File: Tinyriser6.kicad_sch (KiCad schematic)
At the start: 25 parts, among them J1 Bus_M.2_Socket_M, J2 Bus_PCI_Express_x16, J3 Conn_02x04_Odd_Even, M1 Fan_4pin

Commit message: started breaking out all the weird pins
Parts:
- removed TP1: GPU_PWR_EN, TestPoint:TestPoint_Pad_D1.0mm, symbol Connector:TestPoint
- removed TP2: GPU_MACO_EN, TestPoint:TestPoint_Pad_D1.0mm, symbol Connector:TestPoint
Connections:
- net PCIe_CPU_REFCLK1-: now reaches J4.A1 (PCIe_CPU_REFCLK1-)
- net PCIe_CPU_REFCLK5+: now reaches J4.A17 (PCIe_CPU_REFCLK5+)
- net PCIe_CPU_REFCLK5-: now reaches J4.A18 (PCIe_CPU_REFCLK5-)
- net GPU_PWR_EN: now reaches J4.A19 (GPU_PWR_EN)
- net PCIe_CPU_REFCLK1+: now reaches J4.A2 (PCIe_CPU_REFCLK1+)
- net GPU_MACO_EN: now reaches J4.A20 (GPU_MACO_EN)
- net AZ_SDOUT_R: now reaches J4.A21 (AZ_SDOUT_R(ME_DISABLE))
- net ESPI_ALERT0#_BMC: now reaches J4.A22 (ESPI_ALERT0#_BMC@)
- net ESPI_ALERT1#: now reaches J4.A23 (ESPI_ALERT1#@)
- net SIO_SML1ALERT#: now reaches J4.A24 (SIO_SML1ALERT#)
- net ESPI_IO1_BMC: now reaches J4.A25 (ESPI_IO1_BMC@)
- net ESPI_RESET#_BMC: now reaches J4.A26 (ESPI_RESET#_BMC@)
- net ME_RECOVERY_BMC: now reaches J4.A27 (ME_RECOVERY_BMC)
- net SMLINK1_DATA: now reaches J4.A28 (SMLINK1_DATA)
- net SMLINK1_CLK: now reaches J4.A29 (SMLINK1_CLK)
- net PCH_SYSPOWEROK: now reaches J4.A3 (PCH_SYSPOWEROK)
- net PCIE_X8_X4_PRSNT#: now reaches J4.A30 (PCIE_X8_X4_PRSNT#)
- net ESPI_IO0_BMC: now reaches J4.A31 (ESPI_IO0_BMC@)
- net ESPI_CLK_BMC: now reaches J4.A32 (ESPI_CLK_BMC@)
- net BMC_DETECT#: now reaches J4.A4 (BMC_DETECT#(CLKREQ1,5,11,CFG6)@)
- net ESPI_CS1#_BMC: now reaches J4.B1 (@ESPI_CS1#_BMC)
- net ESPI_CS0#_BMC: now reaches J4.B2 (@ESPI_CS0#_BMC)
- net PCIe_CPU_REFCLK11-: now reaches J4.B23 (PCIe_CPU_REFCLK11-)
- net PCIe_CPU_REFCLK11+: now reaches J4.B24 (PCIe_CPU_REFCLK11+)
- net PWRBTN#: now reaches J4.B25 (PWRBTN#)
- net USB_D-: now reaches J4.B26 (USB_D-)
- net USB_D+: now reaches J4.B27 (USB_D+)
- net FP_RST#: now reaches J4.B28 (FP_RST#)
- net +5V: now reaches J4.B3 (+5V_S5)
- net +5V: now also J4.B4 (+5V_S5), J4.B5 (+5V_S5)
- net RSMRST_SIO#: now reaches J4.B6 (RSMRST_SIO#)

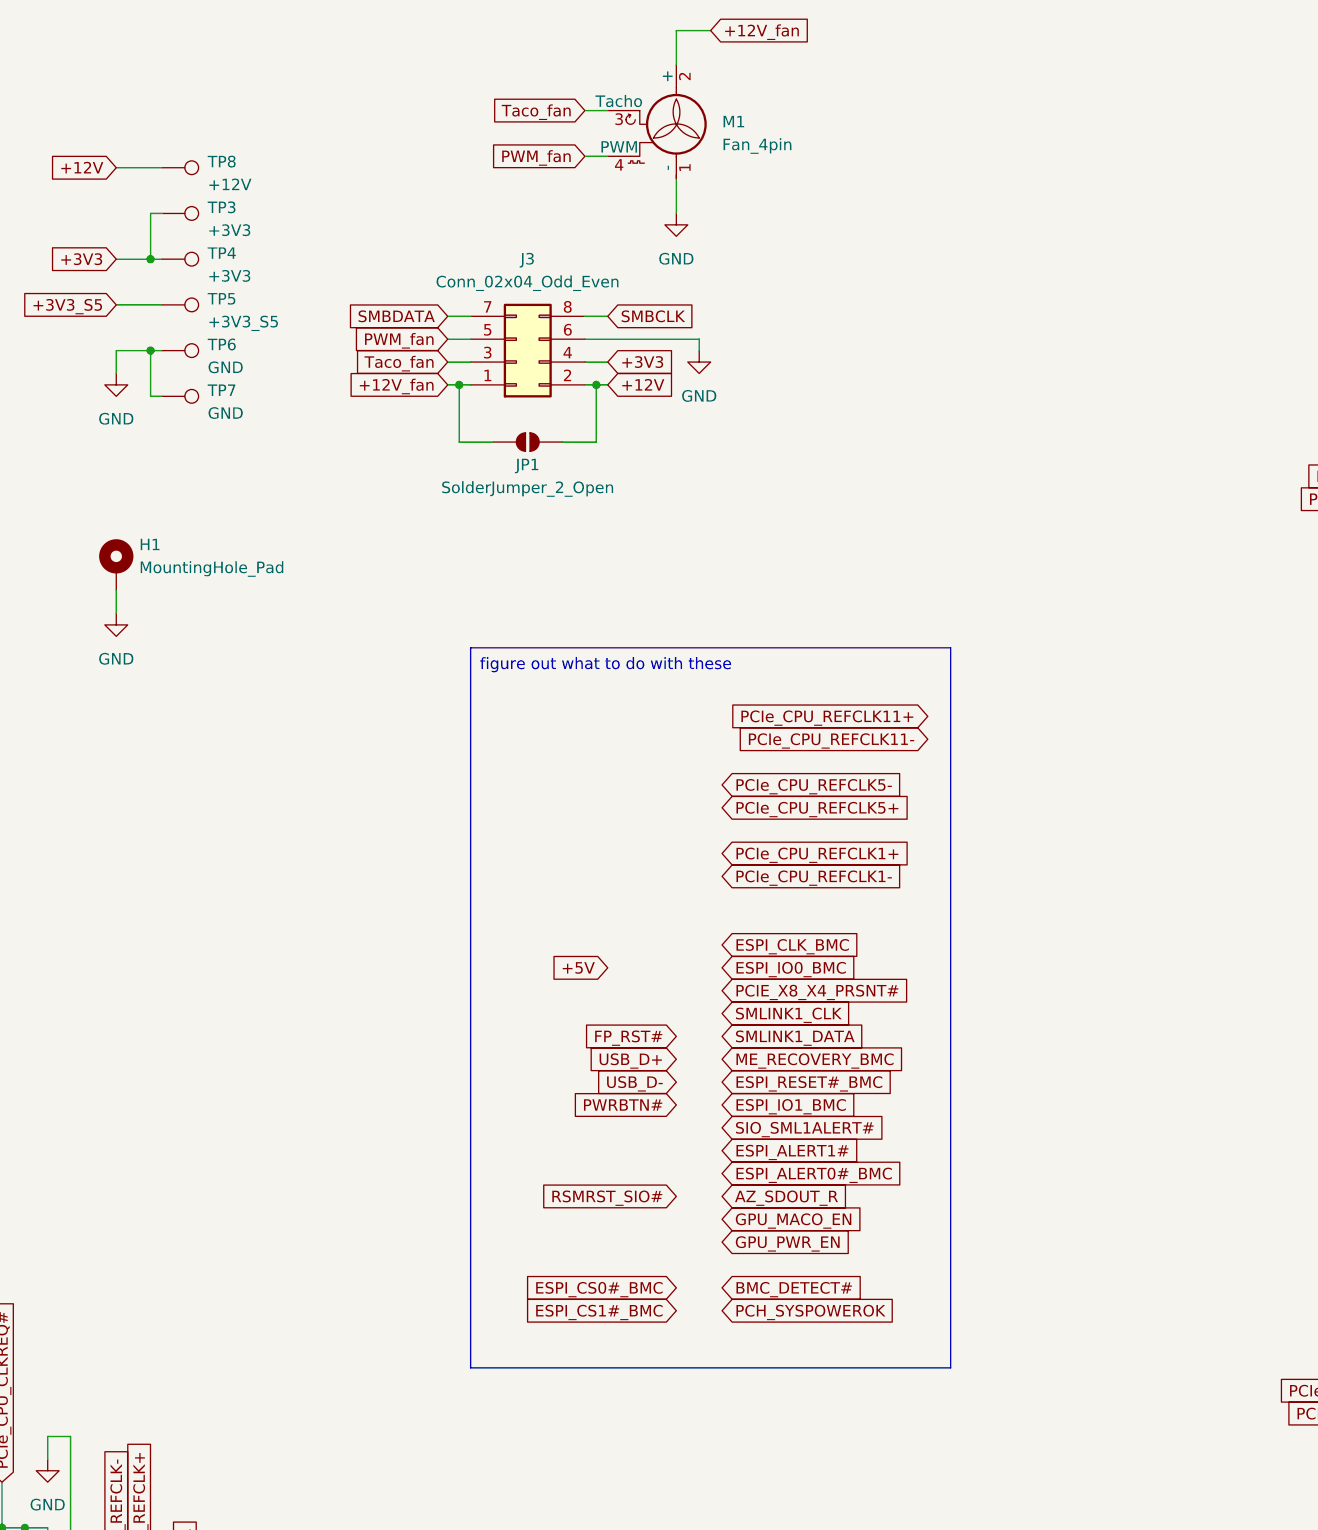
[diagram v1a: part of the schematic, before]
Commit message: Added random io header, usb and started routing M.2 PCIe
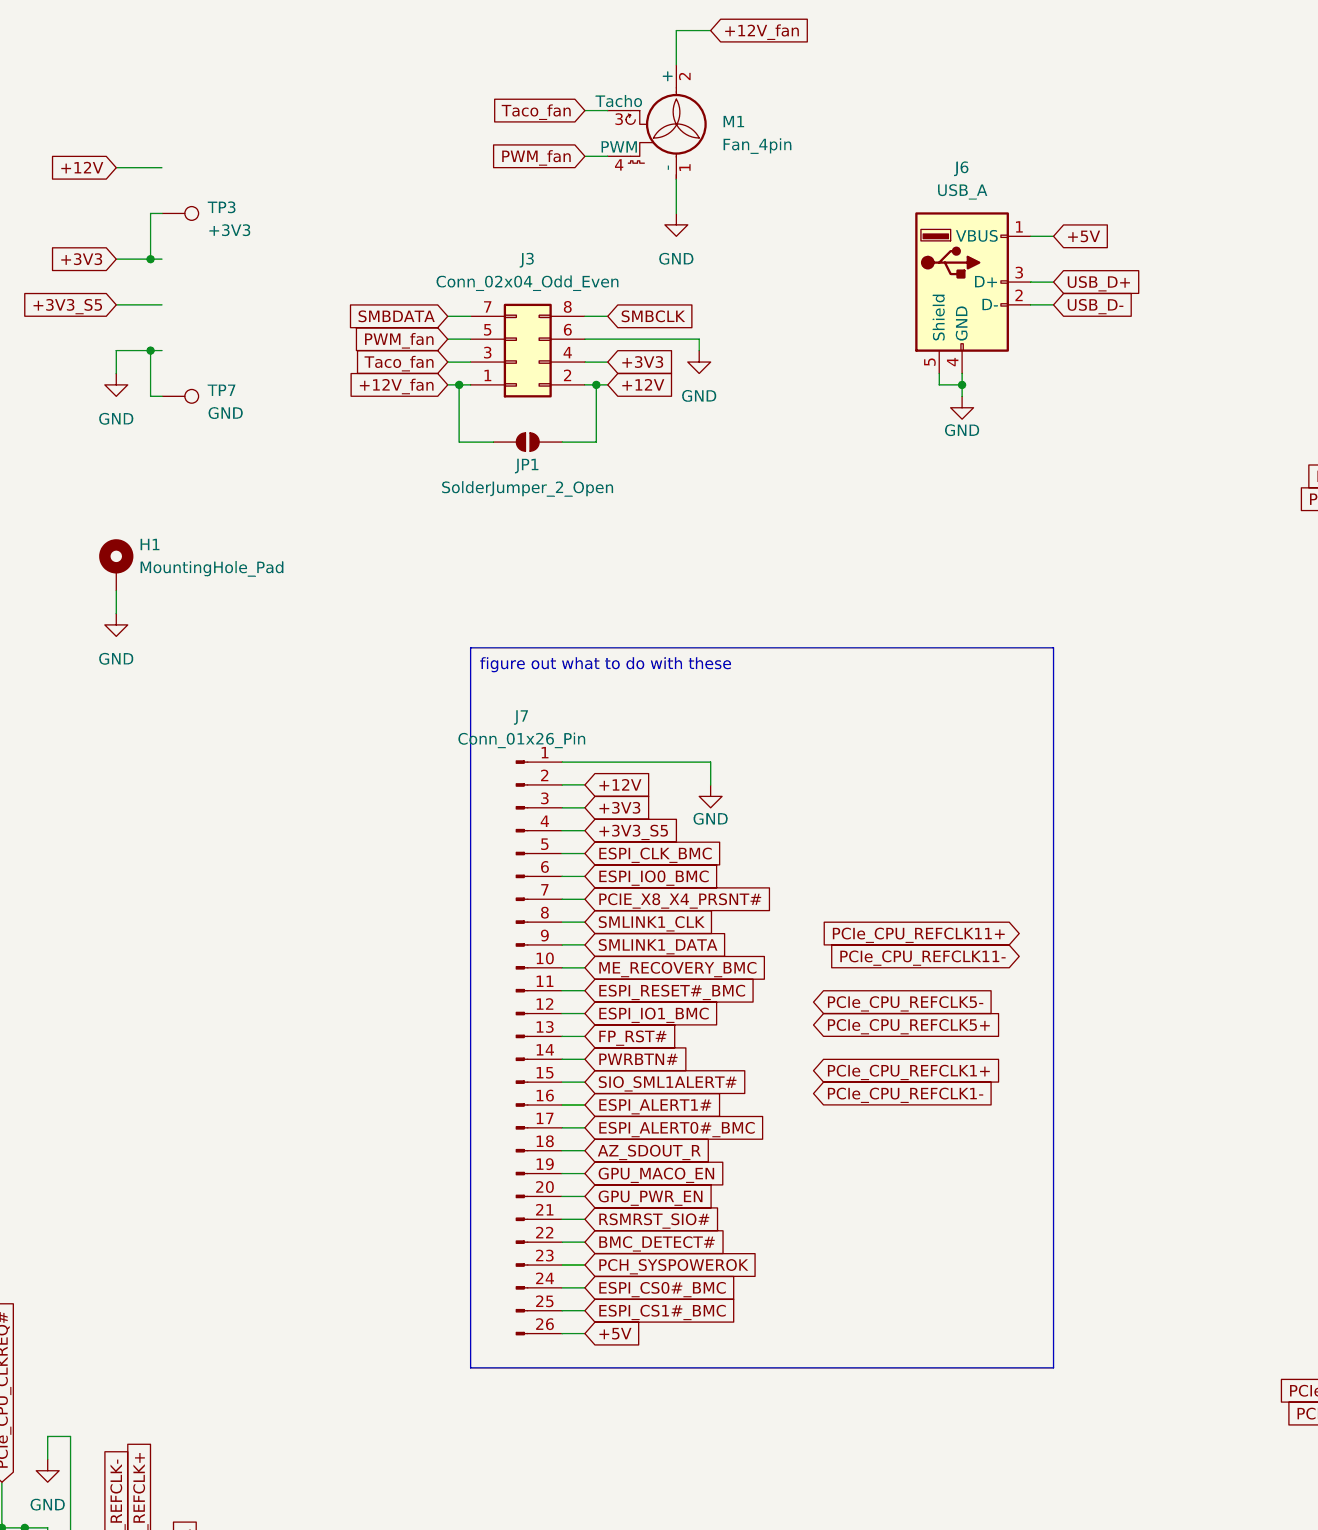
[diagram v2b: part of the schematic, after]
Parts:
- removed TP4: +3V3, TestPoint:TestPoint_THTPad_D1.5mm_Drill0.7mm, symbol Connector:TestPoint
- removed TP5: +3V3_S5, TestPoint:TestPoint_THTPad_D1.5mm_Drill0.7mm, symbol Connector:TestPoint
- removed TP6: GND, TestPoint:TestPoint_THTPad_D1.5mm_Drill0.7mm, symbol Connector:TestPoint
- removed TP8: +12V, TestPoint:TestPoint_THTPad_D1.5mm_Drill0.7mm, symbol Connector:TestPoint
- added J6: USB_A, Connector_USB:USB_A_CONNFLY_DS1095-WNR0, symbol Connector:USB_A
- added J7: Conn_01x26_Pin, Connector_PinHeader_2.00mm:PinHeader_2x13_P2.00mm_Vertical, symbol Connector:Conn_01x26_Pin
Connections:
- net +12V: now also J7.2 (Pin_2)
- net +3V3: now also J7.3 (Pin_3)
- net +3V3_S5: now also J7.4 (Pin_4)
- net +5V: now also J6.1 (VBUS), J7.26 (Pin_26)
- net AZ_SDOUT_R: now also J7.18 (Pin_18)
- net BMC_DETECT#: now also J7.22 (Pin_22)
- net ESPI_ALERT0#_BMC: now also J7.17 (Pin_17)
- net ESPI_ALERT1#: now also J7.16 (Pin_16)
- net ESPI_CLK_BMC: now also J7.5 (Pin_5)
- net ESPI_CS0#_BMC: now also J7.24 (Pin_24)
- net ESPI_CS1#_BMC: now also J7.25 (Pin_25)
- net ESPI_IO0_BMC: now also J7.6 (Pin_6)
- net ESPI_IO1_BMC: now also J7.12 (Pin_12)
- net ESPI_RESET#_BMC: now also J7.11 (Pin_11)
- net FP_RST#: now also J7.13 (Pin_13)
- net GND: now also J6.4 (GND), J6.5 (Shield), J7.1 (Pin_1)
- net GPU_MACO_EN: now also J7.19 (Pin_19)
- net GPU_PWR_EN: now also J7.20 (Pin_20)
- net ME_RECOVERY_BMC: now also J7.10 (Pin_10)
- net PCH_SYSPOWEROK: now also J7.23 (Pin_23)
- net PCIE_X8_X4_PRSNT#: now also J7.7 (Pin_7)
- net PWRBTN#: now also J7.14 (Pin_14)
- net RSMRST_SIO#: now also J7.21 (Pin_21)
- net SIO_SML1ALERT#: now also J7.15 (Pin_15)
- net SMLINK1_CLK: now also J7.8 (Pin_8)
- net SMLINK1_DATA: now also J7.9 (Pin_9)
- net USB_D+: now also J6.3 (D+)
- net USB_D-: now also J6.2 (D-)

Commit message: Trying to figure out what to do with the random io
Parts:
- removed J7: Conn_01x26_Pin, Connector_PinHeader_2.00mm:PinHeader_2x13_P2.00mm_Vertical, symbol Connector:Conn_01x26_Pin
- added J10, J11, J8, J9: Conn_02x04_Odd_Even, Connector_PinHeader_2.00mm:PinHeader_2x04_P2.00mm_Vertical, symbol Connector_Generic:Conn_02x04_Odd_Even
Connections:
- net +3V3: now also J11.1 (Pin_1)
- net +3V3_S5: now also J11.4 (Pin_4)
- net +5V: now also J8.1 (Pin_1)
- net AZ_SDOUT_R: now also J9.3 (Pin_3)
- net BMC_DETECT#: now also J8.4 (Pin_4)
- net ESPI_ALERT0#_BMC: now also J9.4 (Pin_4)
- net ESPI_ALERT1#: now also J9.1 (Pin_1)
- net ESPI_CLK_BMC: now also J11.3 (Pin_3)
- net ESPI_CS0#_BMC: now also J8.6 (Pin_6)
- net ESPI_CS1#_BMC: now also J8.5 (Pin_5)
- net ESPI_IO0_BMC: now also J11.6 (Pin_6)
- net ESPI_IO1_BMC: now also J10.3 (Pin_3)
- net ESPI_RESET#_BMC: now also J10.4 (Pin_4)
- net FP_RST#: now also J10.6 (Pin_6)
- net GND: now also J11.2 (Pin_2)
- net GPU_MACO_EN: now also J9.6 (Pin_6)
- net GPU_PWR_EN: now also J9.5 (Pin_5)
- net ME_RECOVERY_BMC: now also J10.1 (Pin_1)
- net PCH_SYSPOWEROK: now also J8.3 (Pin_3)
- net PCIE_X8_X4_PRSNT#: now also J11.5 (Pin_5)
- net PCIe_CPU_REFCLK1+: now also J8.8 (Pin_8)
- net PCIe_CPU_REFCLK1-: now also J8.7 (Pin_7)
- net PCIe_CPU_REFCLK11+: now also J10.8 (Pin_8)
- net PCIe_CPU_REFCLK11-: now also J10.7 (Pin_7)
- net PCIe_CPU_REFCLK5+: now also J9.7 (Pin_7)
- net PCIe_CPU_REFCLK5-: now also J9.8 (Pin_8)
- net PWRBTN#: now also J10.5 (Pin_5)
- net RSMRST_SIO#: now also J8.2 (Pin_2)
- net SIO_SML1ALERT#: now also J9.2 (Pin_2)
- net SMLINK1_CLK: now also J11.8 (Pin_8)
- net SMLINK1_DATA: now also J11.7 (Pin_7)
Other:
- moved on the sheet: C1, C2, C3, D1, H1, J1, J2, J3, J6, JP1, M1, R1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

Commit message: changed usb port, testing new logo placement
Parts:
- J6: footprint Connector_USB:USB_A_CONNFLY_DS1095-WNR0 -> Connector_USB:USB_A_Wuerth_614004134726_Horizontal

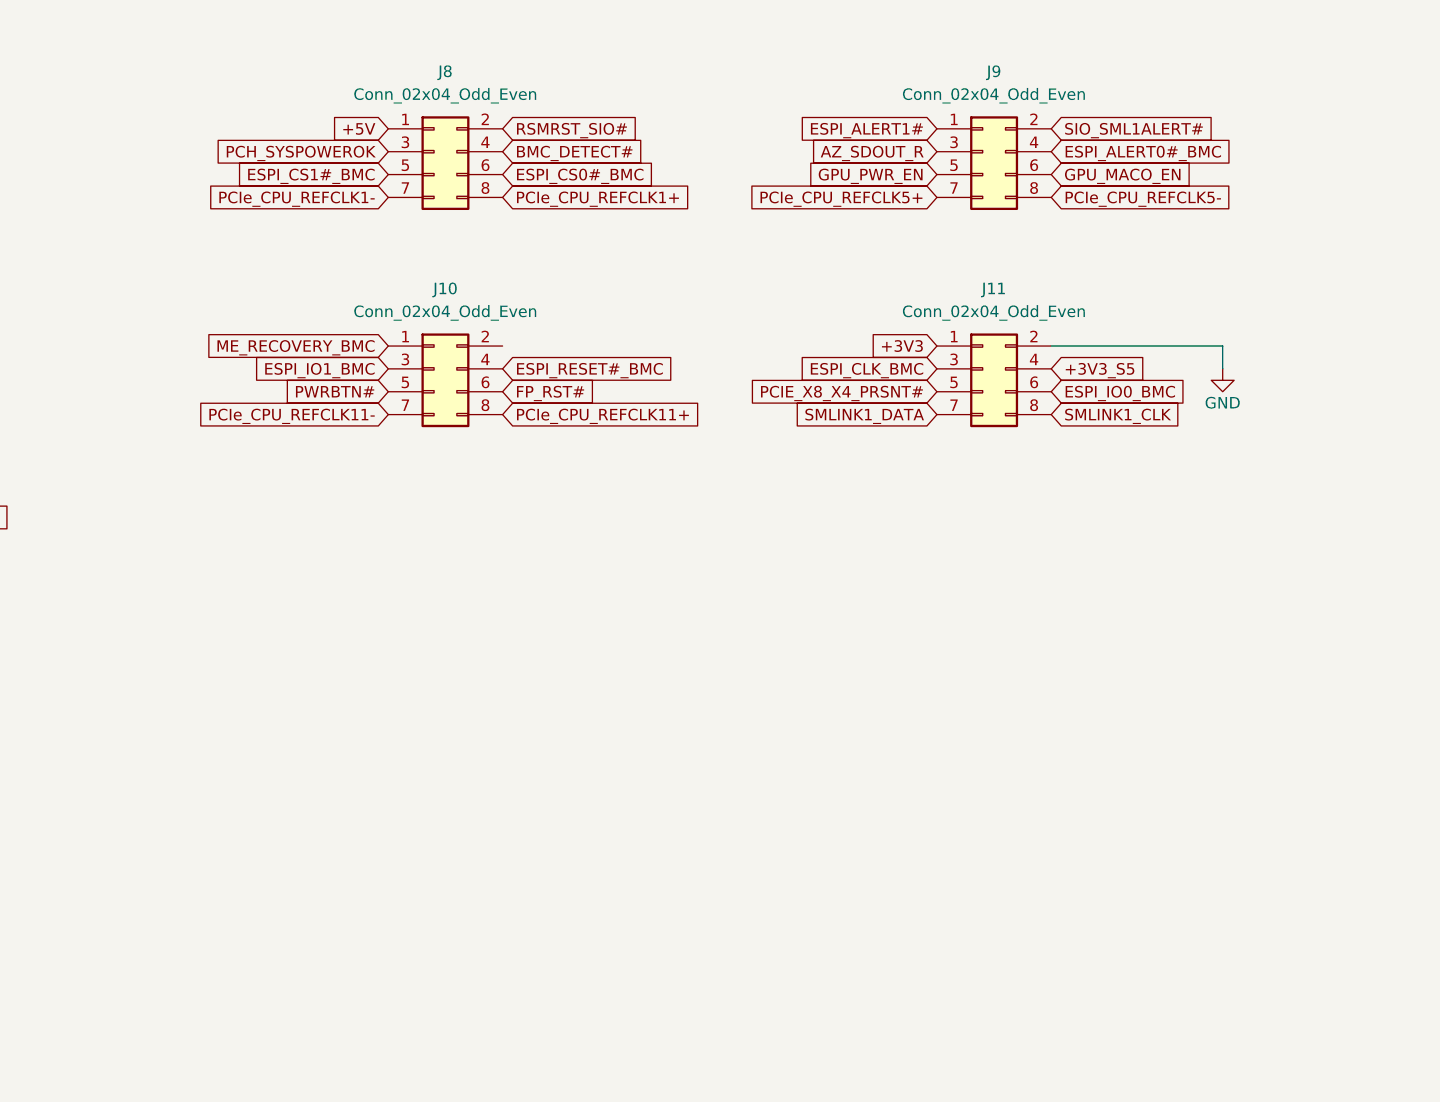
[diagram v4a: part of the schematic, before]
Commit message: giving up on some random IO pins
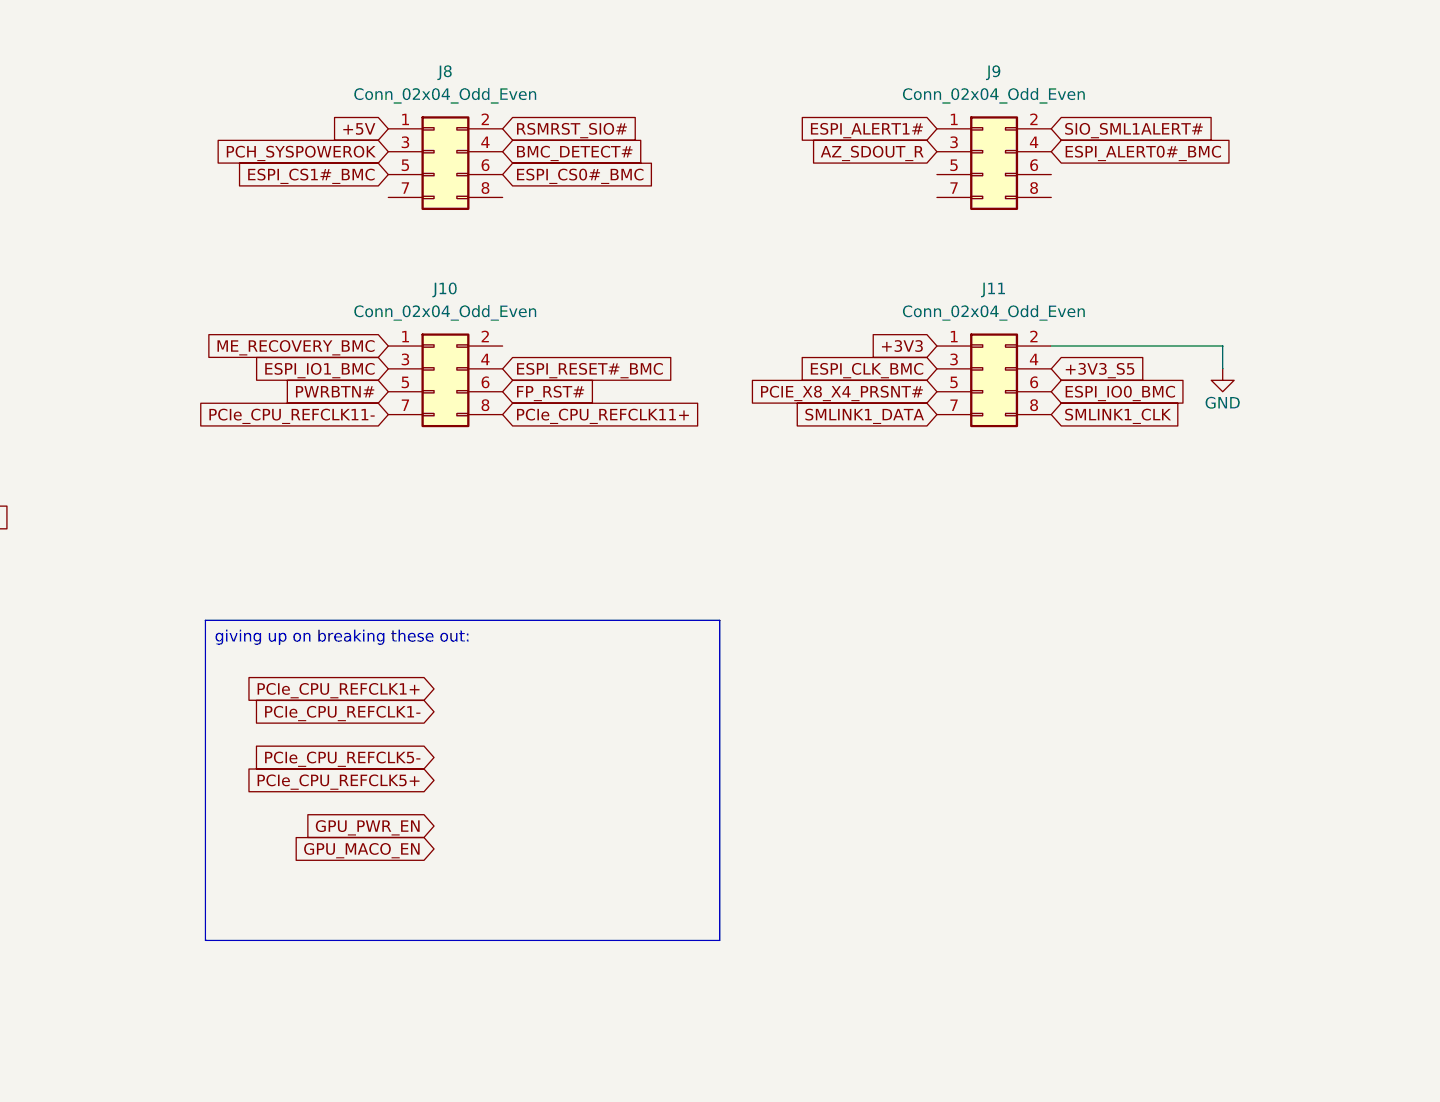
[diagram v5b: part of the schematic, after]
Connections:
- net GPU_MACO_EN: no longer J9.6 (Pin_6)
- net GPU_PWR_EN: no longer J9.5 (Pin_5)
- net PCIe_CPU_REFCLK1+: no longer J8.8 (Pin_8)
- net PCIe_CPU_REFCLK1-: no longer J8.7 (Pin_7)
- net PCIe_CPU_REFCLK5+: no longer J9.7 (Pin_7)
- net PCIe_CPU_REFCLK5-: no longer J9.8 (Pin_8)
